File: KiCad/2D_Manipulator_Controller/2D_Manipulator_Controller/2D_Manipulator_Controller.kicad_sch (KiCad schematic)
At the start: 16 parts, among them J1 282825-2, J2 691311500005, J3 Conn_01x06_Female, J4 691311500004, J5 691311500004, U1 ESP32-DEVKITC-32D, U2 TMC2209_SILENTSTEPSTICK, U3 TMC2209_SILENTSTEPSTICK

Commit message: More progress for 2D manipulator controller
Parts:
- added C3, C4: 100uF, Capacitor_SMD:CP_Elec_8x10, symbol Device:C_Small
- C1, C2: footprint (none) -> Capacitor_SMD:C_1206_3216Metric_Pad1.33x1.80mm_HandSolder
- CAN1: footprint (none) -> SN65HVD230_Module:SN65HSV230_Module
- H1, H2, H3, H4: footprint (none) -> MountingHole:MountingHole_4.3mm_M4
- J1: footprint TE_282825-2 -> 2 Position Terminal Block Header, Male, vertical:phoenix_2Pin_TerminalBlockHeader_male_vertical
- J2: footprint 691311500005 -> 5 Position Terminal Block Header, Male, vertical:phoenix_5Pin_TerminalBlockHeader_male_vertical
- J3: footprint (none) -> Connector_PinHeader_2.54mm:PinHeader_1x06_P2.54mm_Vertical
- J4, J5: footprint 691311500004 -> 4 Position Terminal Block Header, Male, vertical:phoenix_4Pin_TerminalBlockHeader_male_vertical
- R1: renamed from R?; footprint (none) -> Resistor_SMD:R_1206_3216Metric_Pad1.30x1.75mm_HandSolder
- U1: footprint MODULE_ESP32-DEVKITC-32D -> ESP32 DevKit:MODULE_ESP32-DEVKITC-32D
- U2, U3: footprint MODULE_TMC2209_SILENTSTEPSTICK -> TMC2209_SILENTSTEPSTICK:MODULE_TMC2209_SILENTSTEPSTICK
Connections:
- net +24V: now also C3.1, C4.1
- net GND: now also C3.2, C4.2
- net DIAG_0: now reaches U2.JP3_1 (DIAG)
- net DIAG_0: now also U1.34 (IO2)
- net INDEX_0: now reaches U2.JP3_2 (INDEX)
- net INDEX_0: now also U1.33 (IO0)
- net DIAG_1: now reaches U3.JP3_1 (DIAG)
- net DIAG_1: now also U1.13 (IO12)
- net INDEX1: now reaches U3.JP3_2 (INDEX)
- net INDEX1: now also U1.12 (IO14)
- no-connect marks 17 -> 19

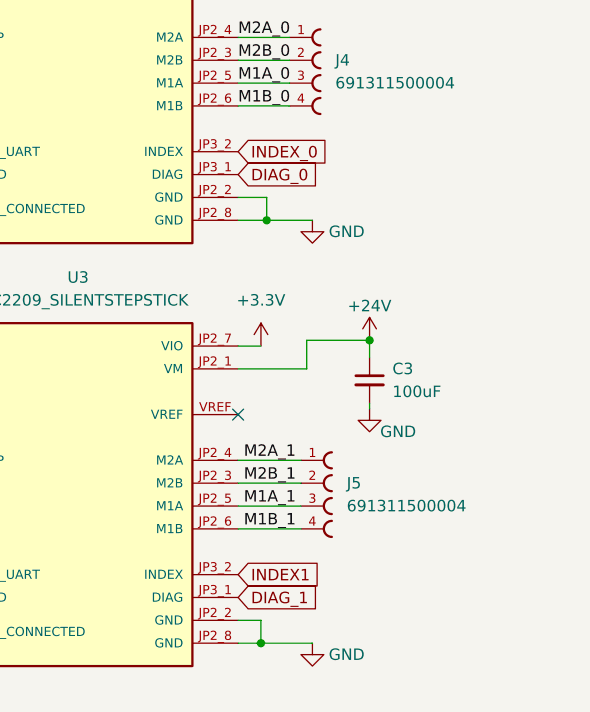
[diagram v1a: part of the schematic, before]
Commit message: Adding 10k pullup resistors to diag pins
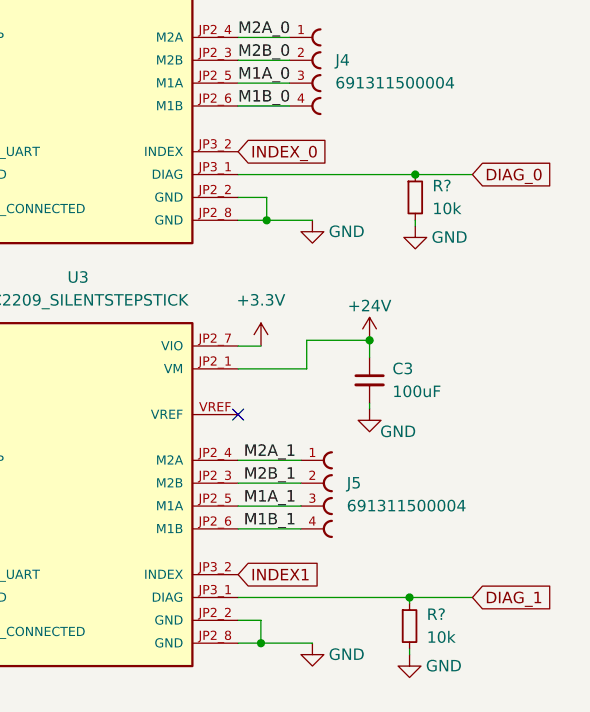
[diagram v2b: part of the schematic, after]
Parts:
- added R? (x2): 10k, symbol Device:R_Small
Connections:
- net DIAG_0: now also R?.1
- net DIAG_1: now also R?.1
- net GND: now also R?.2, R?.2
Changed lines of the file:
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@@
   (junction (at 135.255 19.685) (diameter 0) (color 0 0 0 0)
   )
+  (junction (at 269.24 71.12) (diameter 0) (color 0 0 0 0)
+  )
   (junction (at 135.255 29.845) (diameter 0) (color 0 0 0 0)
+  )
+  (junction (at 268.605 118.11) (diameter 0) (color 0 0 0 0)
   )
   (junction (at 107.95 105.41) (diameter 0) (color 0 0 0 0)
@@
     (stroke (width 0) (type default) (color 0 0 0 0))
   )
+  (wire (pts (xy 268.605 118.745) (xy 268.605 118.11))
+    (stroke (width 0) (type default) (color 0 0 0 0))
+  )
   (wire (pts (xy 264.16 89.535) (xy 264.16 91.44))
     (stroke (width 0) (type default) (color 0 0 0 0))
@@
     (stroke (width 0) (type default) (color 0 0 0 0))
   )
+  (wire (pts (xy 269.24 71.12) (xy 249.555 71.12))
+    (stroke (width 0) (type default) (color 0 0 0 0))
+  )
   (wire (pts (xy 57.15 115.57) (xy 71.12 115.57))
     (stroke (width 0) (type default) (color 0 0 0 0))
@@
     (stroke (width 0) (type default) (color 0 0 0 0))
   )
+  (wire (pts (xy 275.59 118.11) (xy 268.605 118.11))
+    (stroke (width 0) (type default) (color 0 0 0 0))
+  )
   (wire (pts (xy 154.94 90.17) (xy 158.115 90.17))
     (stroke (width 0) (type default) (color 0 0 0 0))
@@
     (stroke (width 0) (type default) (color 0 0 0 0))
   )
+  (wire (pts (xy 268.605 118.11) (xy 249.555 118.11))
+    (stroke (width 0) (type default) (color 0 0 0 0))
+  )
   (wire (pts (xy 257.175 92.71) (xy 257.175 89.535))
     (stroke (width 0) (type default) (color 0 0 0 0))
@@
     (stroke (width 0) (type default) (color 0 0 0 0))
   )
+  (wire (pts (xy 268.605 123.825) (xy 268.605 124.46))
+    (stroke (width 0) (type default) (color 0 0 0 0))
+  )
   (wire (pts (xy 249.555 105.41) (xy 256.54 105.41))
     (stroke (width 0) (type default) (color 0 0 0 0))
@@
     (stroke (width 0) (type default) (color 0 0 0 0))
   )
+  (wire (pts (xy 275.59 71.12) (xy 269.24 71.12))
+    (stroke (width 0) (type default) (color 0 0 0 0))
+  )
   (wire (pts (xy 249.555 107.95) (xy 256.54 107.95))
     (stroke (width 0) (type default) (color 0 0 0 0))
@@
   )
   (wire (pts (xy 201.295 107.95) (xy 201.295 106.68))
+    (stroke (width 0) (type default) (color 0 0 0 0))
+  )
+  (wire (pts (xy 269.24 76.2) (xy 269.24 76.835))
     (stroke (width 0) (type default) (color 0 0 0 0))
   )
@@
     )
   )
-  (global_label "DIAG_1" (shape input) (at 249.555 118.11 0) (fields_autoplaced)
-    (effects (font (size 1.27 1.27)) (justify left))
-    (property "Intersheet References" "${INTERSHEET_REFS}" (id 0) (at 258.3786 118.0306 0)
-      (effects (font (size 1.27 1.27)) (justify left) hide)
-    )
-  )
-  (global_label "DIAG_0" (shape input) (at 249.555 71.12 0) (fields_autoplaced)
-    (effects (font (size 1.27 1.27)) (justify left))
-    (property "Intersheet References" "${INTERSHEET_REFS}" (id 0) (at 258.3786 71.0406 0)
+  (global_label "DIAG_1" (shape input) (at 275.59 118.11 0) (fields_autoplaced)
+    (effects (font (size 1.27 1.27)) (justify left))
+    (property "Intersheet References" "${INTERSHEET_REFS}" (id 0) (at 284.4136 118.0306 0)
+      (effects (font (size 1.27 1.27)) (justify left) hide)
+    )
+  )
+  (global_label "DIAG_0" (shape input) (at 275.59 71.12 0) (fields_autoplaced)
+    (effects (font (size 1.27 1.27)) (justify left))
+    (property "Intersheet References" "${INTERSHEET_REFS}" (id 0) (at 284.4136 71.0406 0)
       (effects (font (size 1.27 1.27)) (justify left) hide)
     )
@@
     (pin "1")
   )
+  (symbol (lib_id "Device:R_Small") (at 268.605 121.285 0) (unit 1)
+    (in_bom yes) (on_board yes) (fields_autoplaced)
+    (property "Reference" "R?" (id 0) (at 270.51 120.0149 0)
+      (effects (font (size 1.27 1.27)) (justify left))
+    )
+    (property "Value" "10k" (id 1) (at 270.51 122.5549 0)
+      (effects (font (size 1.27 1.27)) (justify left))
+    )
+    (property "Footprint" "" (id 2) (at 268.605 121.285 0)
+      (effects (font (size 1.27 1.27)) hide)
+    )
+    (property "Datasheet" "~" (id 3) (at 268.605 121.285 0)
+      (effects (font (size 1.27 1.27)) hide)
+    )
+    (pin "1")
+    (pin "2")
+  )
   (symbol (lib_id "Connector:Conn_01x06_Female") (at 52.07 120.65 0) (mirror y) (unit 1)
     (in_bom yes) (on_board yes) (fields_autoplaced)
@@
     )
   )
+  (symbol (lib_id "power:GND") (at 268.605 124.46 0) (unit 1)
+    (in_bom yes) (on_board yes)
+    (property "Reference" "#PWR?" (id 0) (at 268.605 130.81 0)
+      (effects (font (size 1.27 1.27)) hide)
+    )
+    (property "Value" "GND" (id 1) (at 272.415 125.73 0))
+    (property "Footprint" "" (id 2) (at 268.605 124.46 0)
+      (effects (font (size 1.27 1.27)) hide)
+    )
+    (property "Datasheet" "" (id 3) (at 268.605 124.46 0)
+      (effects (font (size 1.27 1.27)) hide)
+    )
+    (pin "1")
+  )
   (symbol (lib_id "power:GND") (at 208.915 110.49 0) (unit 1)
     (in_bom yes) (on_board yes)
@@
       (effects (font (size 1.27 1.27)) hide)
     )
+  )
+  (symbol (lib_id "power:GND") (at 269.24 76.835 0) (unit 1)
+    (in_bom yes) (on_board yes)
+    (property "Reference" "#PWR?" (id 0) (at 269.24 83.185 0)
+      (effects (font (size 1.27 1.27)) hide)
+    )
+    (property "Value" "GND" (id 1) (at 273.05 78.105 0))
+    (property "Footprint" "" (id 2) (at 269.24 76.835 0)
+      (effects (font (size 1.27 1.27)) hide)
+    )
+    (property "Datasheet" "" (id 3) (at 269.24 76.835 0)
+      (effects (font (size 1.27 1.27)) hide)
+    )
+    (pin "1")
   )
   (symbol (lib_id "Device:R_Small") (at 185.42 85.09 0) (unit 1)
@@
     (pin "2")
   )
+  (symbol (lib_id "Device:R_Small") (at 269.24 73.66 0) (unit 1)
+    (in_bom yes) (on_board yes) (fields_autoplaced)
+    (property "Reference" "R?" (id 0) (at 271.145 72.3899 0)
+      (effects (font (size 1.27 1.27)) (justify left))
+    )
+    (property "Value" "10k" (id 1) (at 271.145 74.9299 0)
+      (effects (font (size 1.27 1.27)) (justify left))
+    )
+    (property "Footprint" "" (id 2) (at 269.24 73.66 0)
+      (effects (font (size 1.27 1.27)) hide)
+    )
+    (property "Datasheet" "~" (id 3) (at 269.24 73.66 0)
+      (effects (font (size 1.27 1.27)) hide)
+    )
+    (pin "1")
+    (pin "2")
+  )
   (sheet_instances
     (path "/" (page "1"))
@@
       (reference "#PWR0124") (unit 1) (value "GND") (footprint "")
     )
+    (path "/9be869b6-351d-4e16-aee0-2bfe5c0243cc"
+      (reference "#PWR?") (unit 1) (value "GND") (footprint "")
+    )
+    (path "/dd7d35e6-4f84-4644-8ff1-ae53b19ef62c"
+      (reference "#PWR?") (unit 1) (value "GND") (footprint "")
+    )
     (path "/5a24f3d2-64b3-4301-9d5e-b6230e1cb27a"
       (reference "C1") (unit 1) (value "10uF") (footprint "Capacitor_SMD:C_1206_3216Metric_Pad1.33x1.80mm_HandSolder")
@@
       (reference "R1") (unit 1) (value "1k") (footprint "Resistor_SMD:R_1206_3216Metric_Pad1.30x1.75mm_HandSolder")
     )
+    (path "/411bba45-62d4-44fd-a855-683c3df0a6df"
+      (reference "R?") (unit 1) (value "10k") (footprint "")
+    )
+    (path "/fb552787-147e-4edf-8cbf-99d076f479c4"
+      (reference "R?") (unit 1) (value "10k") (footprint "")
+    )
     (path "/f6662114-e94f-4466-8b01-5f4d76363a86"
